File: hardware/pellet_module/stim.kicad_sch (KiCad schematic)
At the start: 44 parts, among them J11 Conn_Coaxial, J12 Conn_01x02_Pin, J13 Conn_01x02_Pin, J14 Conn_01x02_Pin, J15 Conn_Coaxial, J16 Conn_Coaxial, J17 Conn_Coaxial, J18 Conn_Coaxial, J19 Conn_01x02_Pin, J21 Conn_Coaxial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

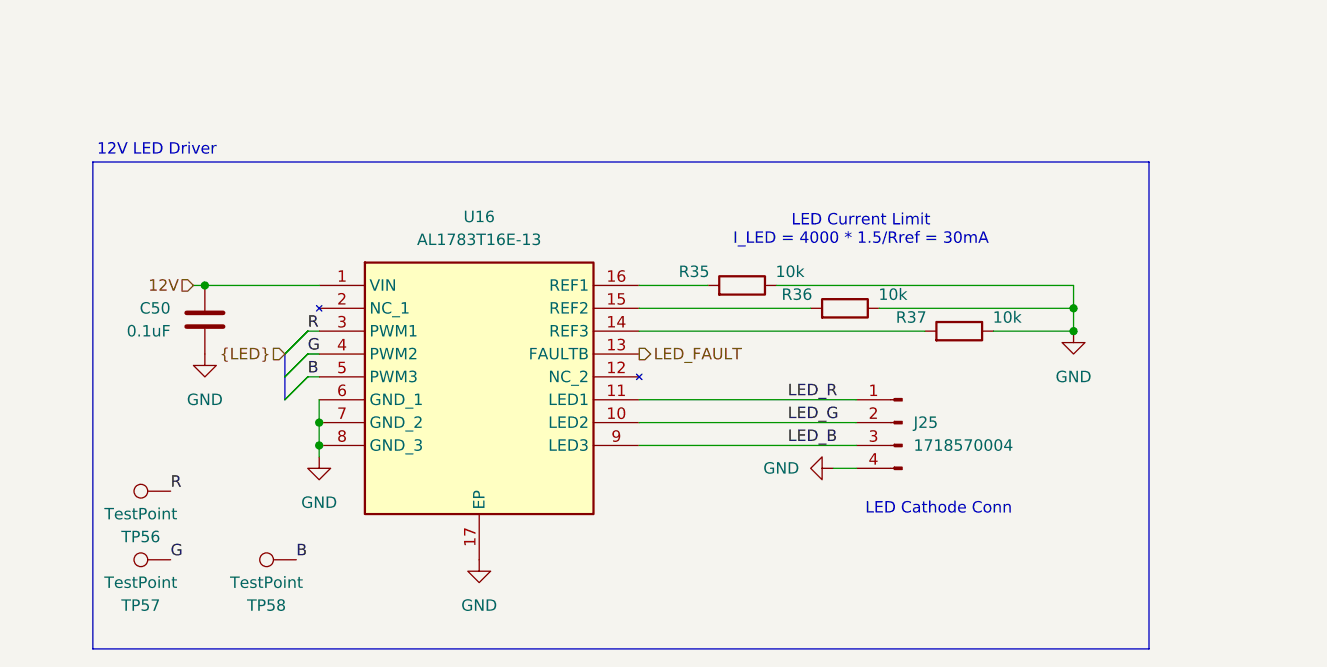
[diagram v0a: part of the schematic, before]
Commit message: Switch to high-side LED driver
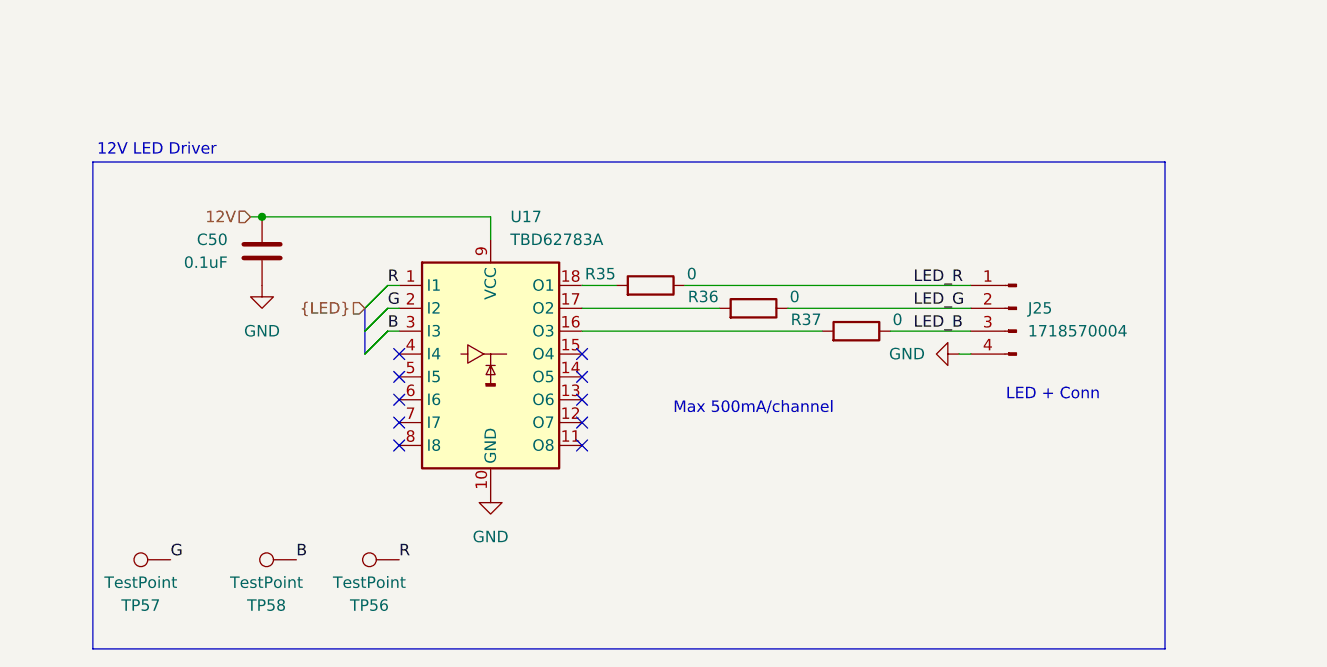
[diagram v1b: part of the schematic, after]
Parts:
- removed U16: AL1783T16E-13, Leaf_LEDs:SOP65P640X108-17N, symbol Leaf_LEDs:AL1783T16E-13
- added U17: TBD62783A, Package_SO:SOIC-18W_7.5x11.6mm_P1.27mm, symbol Transistor_Array:TBD62783A
- R35, R36, R37: value 10k -> 0; LCSC C25804 -> C21189; MPN 0603WAF1002T5E -> 0603WAF0000T5E
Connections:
- net 12V: now also U17.9 (VCC)
- net B: now also U17.3 (I3)
- net G: now also U17.2 (I2)
- net GND: now also U17.10 (GND); no longer R35.1, R36.1, R37.1
- net LED_B: now also R37.1
- net LED_G: now also R36.1
- net LED_R: now also R35.1
- net R: now also U17.1 (I1)
- net at R37.2: now also U17.16 (O3)
- net at R36.2: now also U17.17 (O2)
- net at R35.2: now also U17.18 (O1)
- no-connect marks 0 -> 10
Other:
- note added: "LED + Conn"
- note added: "Max 500mA/channel"
- note removed: "LED Cathode Conn"
- note removed: "LED Current Limit I_LED = 4000 * 1.5/Rref = 30mA"
- moved on the sheet: C50, J25, TP56

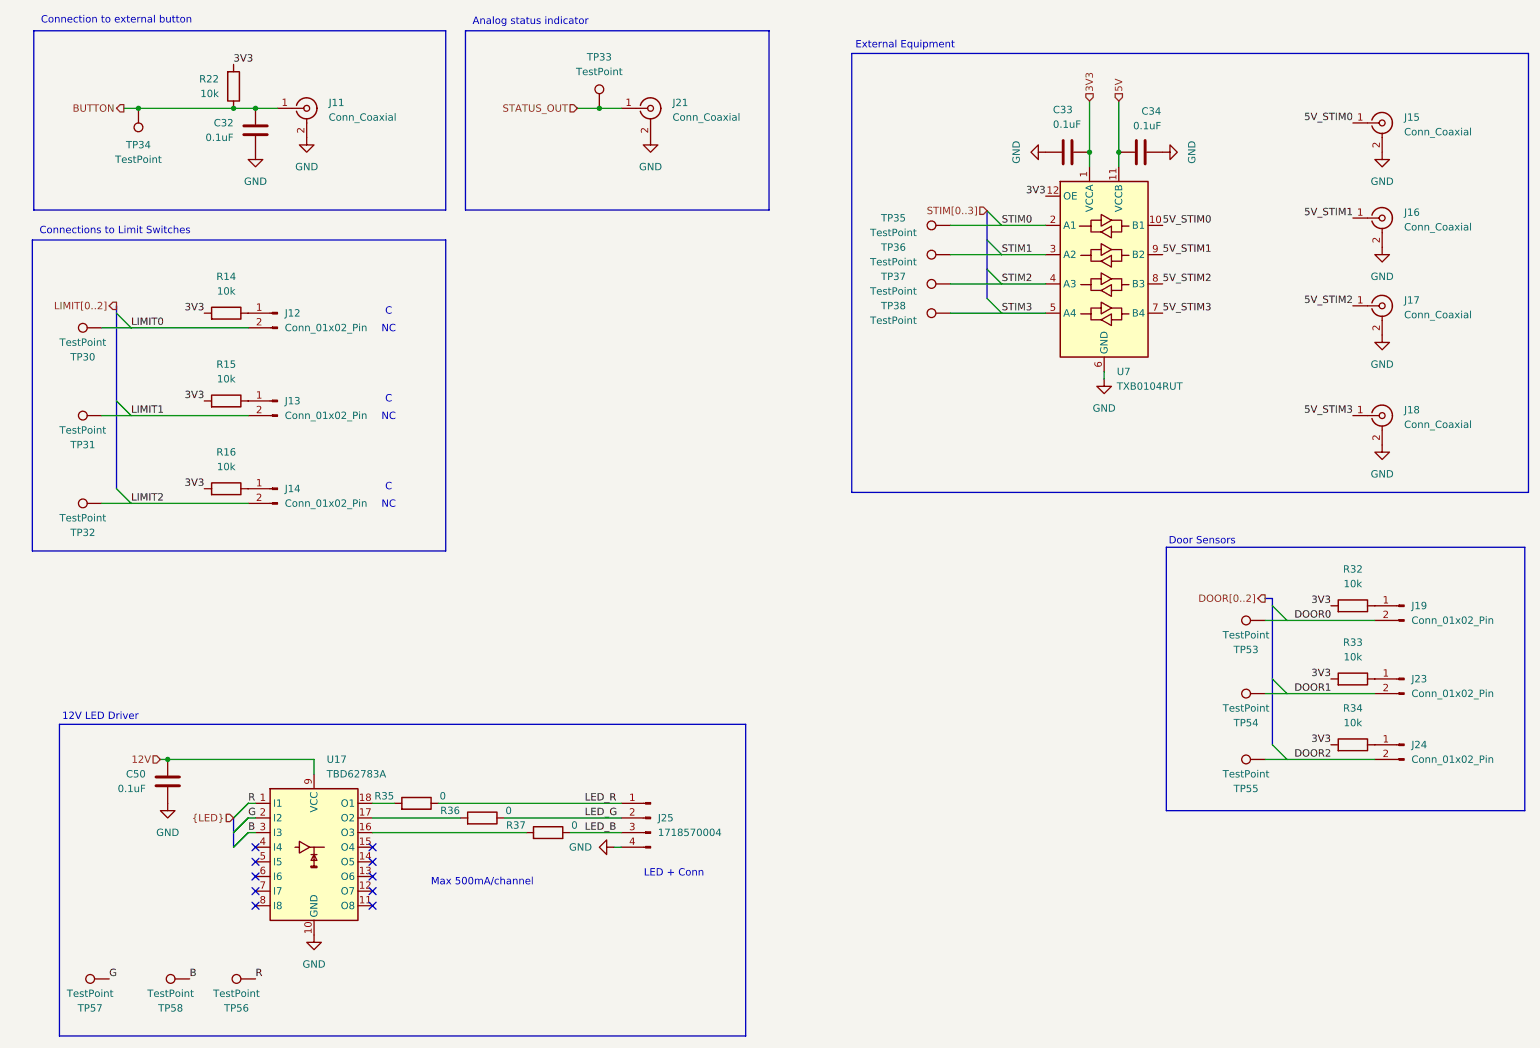
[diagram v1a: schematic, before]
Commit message: Fixes based on discovered issues on testing rig
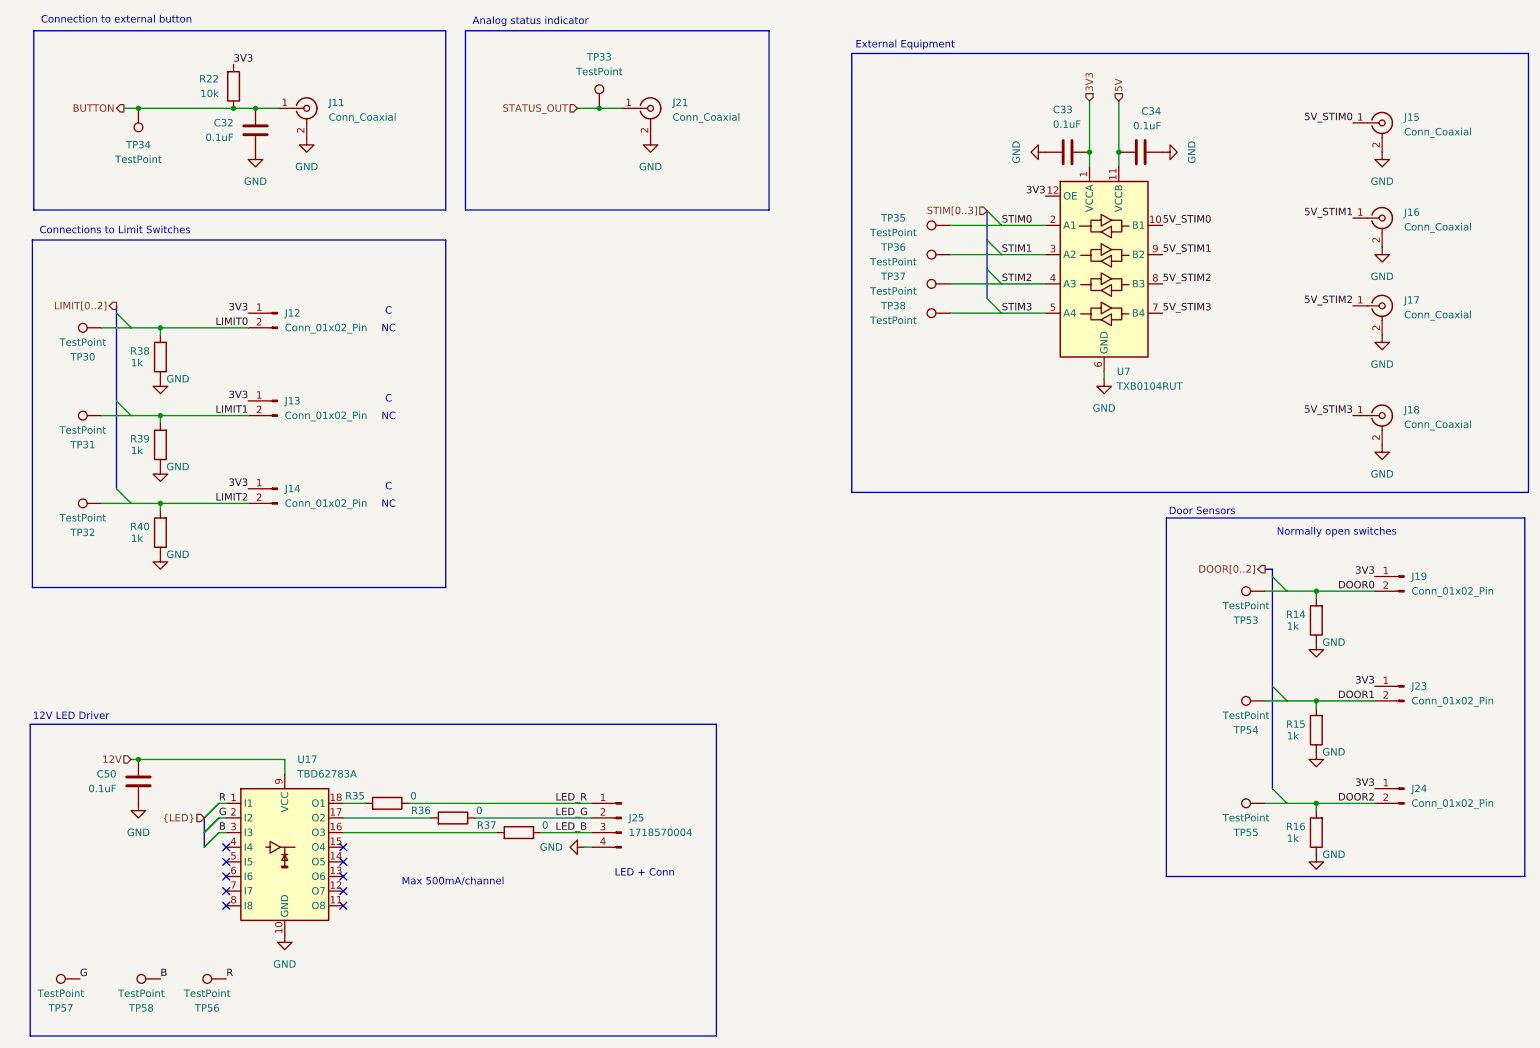
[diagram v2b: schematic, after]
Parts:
- removed R32, R33, R34: 10k, Resistor_SMD:R_0603_1608Metric, symbol Device:R
- added R38, R39, R40: 1k, Resistor_SMD:R_0603_1608Metric, symbol Device:R
- R14, R15, R16: value 10k -> 1k; LCSC C25804 -> C21190; MPN 0603WAF1002T5E -> 0603WAF1001T5E
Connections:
- net 3V3: now also J12.1 (Pin_1), J13.1 (Pin_1), J14.1 (Pin_1), J19.1 (Pin_1), J23.1 (Pin_1), J24.1 (Pin_1); no longer R14.2, R15.2, R16.2
- net DOOR0: now also R14.2
- net DOOR1: now also R15.2
- net DOOR2: now also R16.2
- net GND: now also R14.1, R15.1, R16.1, R38.1, R39.1, R40.1
- net LIMIT0: now also R38.2
- net LIMIT1: now also R39.2
- net LIMIT2: now also R40.2
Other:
- note added: "Normally open switches"
- moved on the sheet: C50, J19, J23, J24, J25, R35, R36, R37, TP53, TP54, TP55, TP56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

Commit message: Fix connection error on BNC connector, clean DRC for everything
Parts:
- J11, J15, J16, J17, J18, J21: footprint Leaf_Connectors:Conn_BNC_KH-801-0038 -> Leaf_Connectors:Conn_BNC_KH-BNC50-3511
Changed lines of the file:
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@@
 	(title_block
 		(title "Autotrainer Pellet Module - External IO")
-		(date "2024-11-18")
+		(date "2024-11-25")
 		(rev "v1.2")
 		(company "Christie Lab, CU-Anschutz")
@@
 			)
 		)
-		(property "Footprint" "Leaf_Connectors:Conn_BNC_KH-801-0038"
+		(property "Footprint" "Leaf_Connectors:Conn_BNC_KH-BNC50-3511"
 			(at 62.23 30.48 0)
 			(effects
@@
 			)
 		)
-		(property "Footprint" "Leaf_Connectors:Conn_BNC_KH-801-0038"
+		(property "Footprint" "Leaf_Connectors:Conn_BNC_KH-BNC50-3511"
 			(at 121.92 30.48 0)
 			(effects
@@
 			)
 		)
-		(property "Footprint" "Leaf_Connectors:Conn_BNC_KH-801-0038"
+		(property "Footprint" "Leaf_Connectors:Conn_BNC_KH-BNC50-3511"
 			(at 248.92 49.53 0)
 			(effects
@@
 			)
 		)
-		(property "Footprint" "Leaf_Connectors:Conn_BNC_KH-801-0038"
+		(property "Footprint" "Leaf_Connectors:Conn_BNC_KH-BNC50-3511"
 			(at 248.92 64.77 0)
 			(effects
@@
 			)
 		)
-		(property "Footprint" "Leaf_Connectors:Conn_BNC_KH-801-0038"
+		(property "Footprint" "Leaf_Connectors:Conn_BNC_KH-BNC50-3511"
 			(at 248.92 33.02 0)
 			(effects
@@
 			)
 		)
-		(property "Footprint" "Leaf_Connectors:Conn_BNC_KH-801-0038"
+		(property "Footprint" "Leaf_Connectors:Conn_BNC_KH-BNC50-3511"
 			(at 248.92 83.82 0)
 			(effects
